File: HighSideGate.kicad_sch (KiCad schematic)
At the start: 15 parts, among them J6 VOUT, Q5 Q_NMOS_GDS, U3 IRS2075

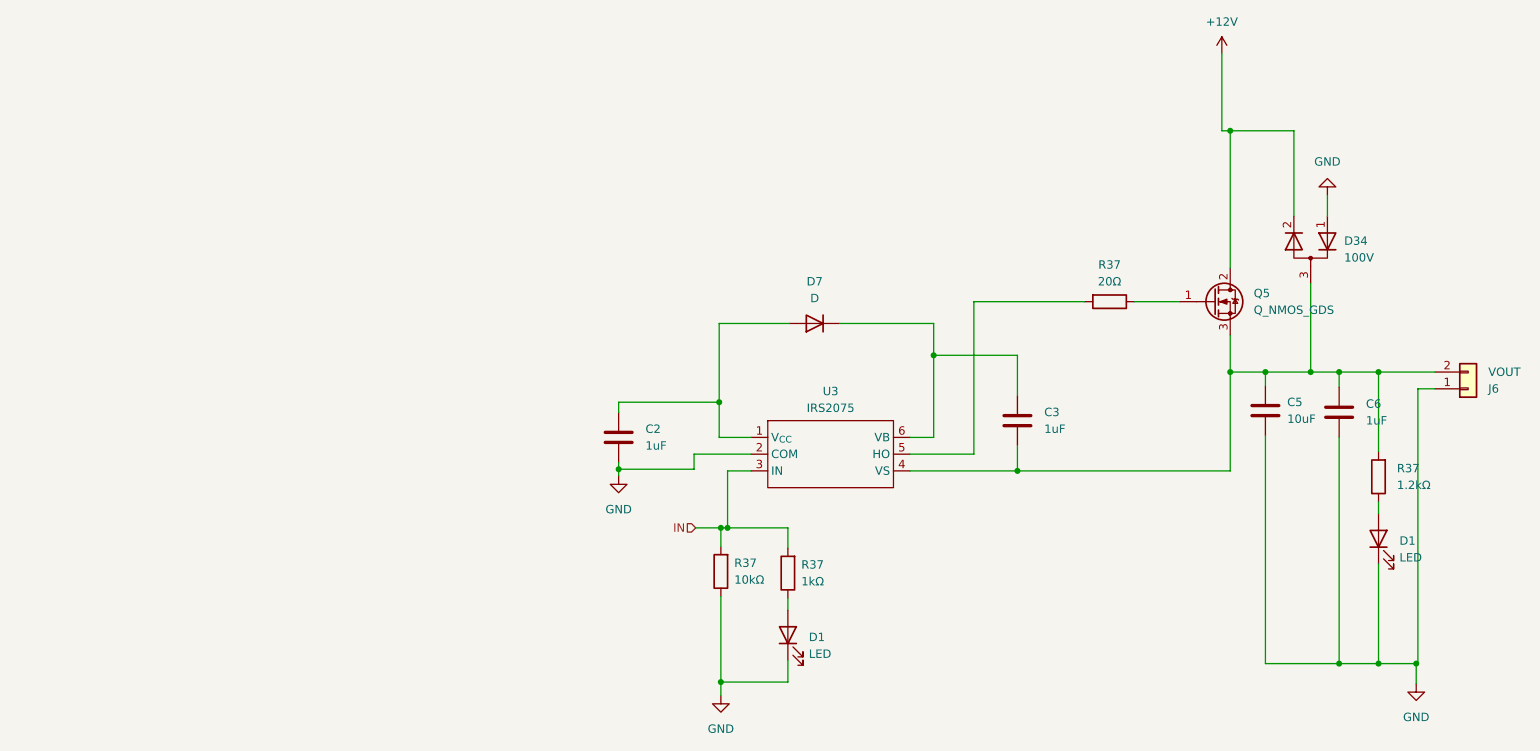
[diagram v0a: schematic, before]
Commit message: Fixed FETs on input.
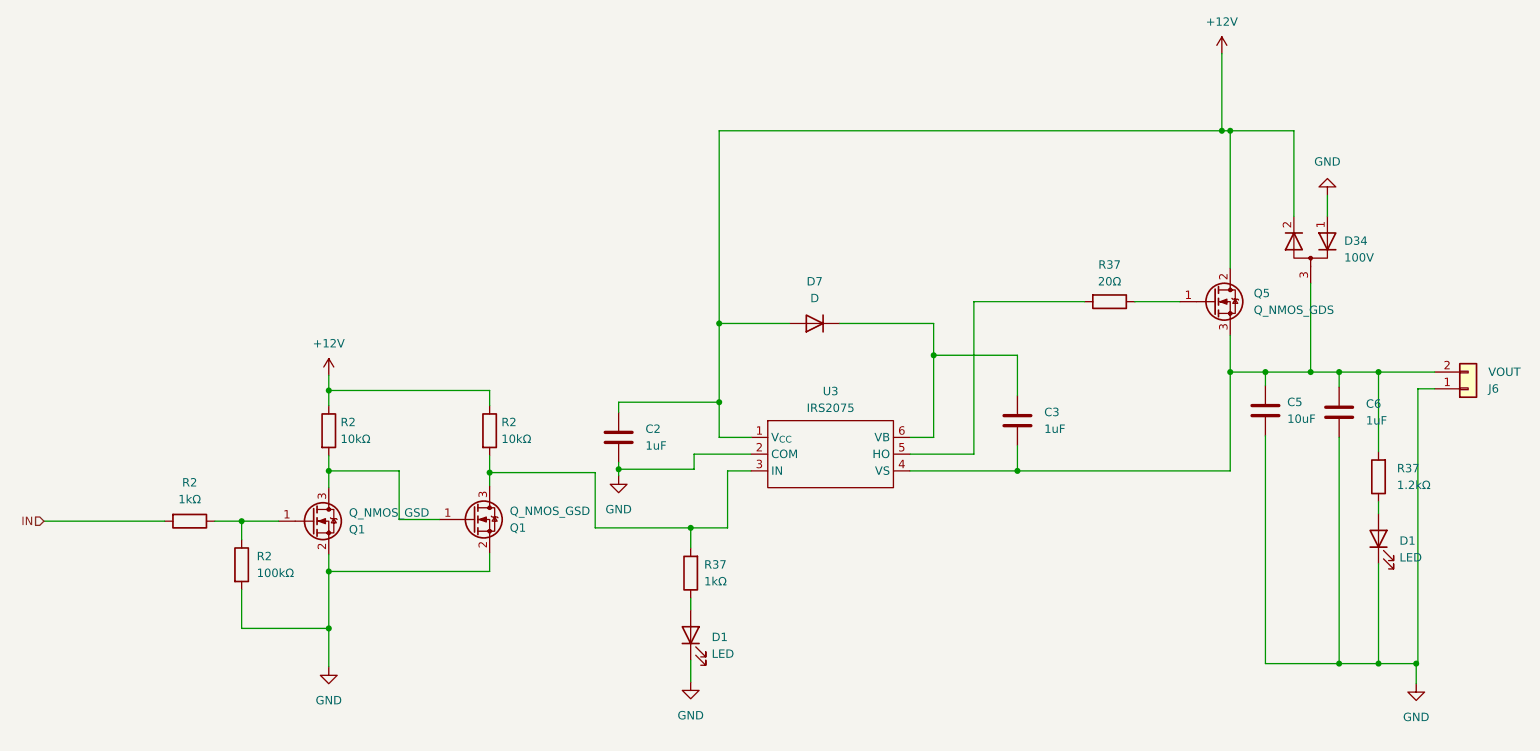
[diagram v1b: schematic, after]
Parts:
- removed R37: 10kΩ, Resistor_SMD:R_0805_2012Metric, symbol Device:R
- added Q1 (x2): Q_NMOS_GSD, Package_TO_SOT_SMD:SOT-23, symbol Device:Q_NMOS_GSD
- added R2: 1kΩ, Resistor_SMD:R_0805_2012Metric, symbol Device:R
- added R2 (x2): 10kΩ, Resistor_SMD:R_0805_2012Metric, symbol Device:R
- added R2: 100kΩ, Resistor_SMD:R_0805_2012Metric, symbol Device:R
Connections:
- net +12V: now also C2.1, D7.2 (A), U3.1 (V_{CC}), R2.1, R2.1
- net GND: now also Q1.2 (S), Q1.2 (S), R2.2
- net IN: now also R2.2; no longer R37.2, U3.3 (IN)
- new net: Q1.1 (G), R2.1, R2.1
- new net: Q1.1 (G), Q1.3 (D), R2.2
- new net: Q1.3 (D), R2.2, R37.2, U3.3 (IN)
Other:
- moved on the sheet: D1, R37
